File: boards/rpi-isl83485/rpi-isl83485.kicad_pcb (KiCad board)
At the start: 2 copper layers, 25.9 x 15.2 mm, 10 parts, among them J1 RPi, J2 Conn_01x03, J3 JST-GH, U1 ISL83485

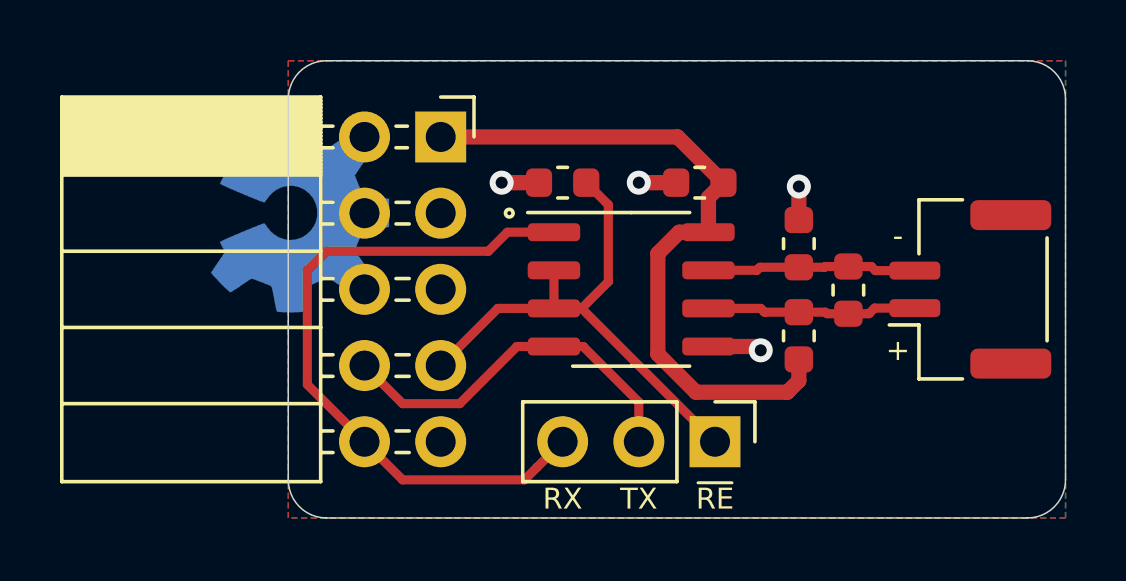
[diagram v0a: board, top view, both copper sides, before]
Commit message: Added FT2232H breakout for programming /boards/ice40hx8k-bg121/
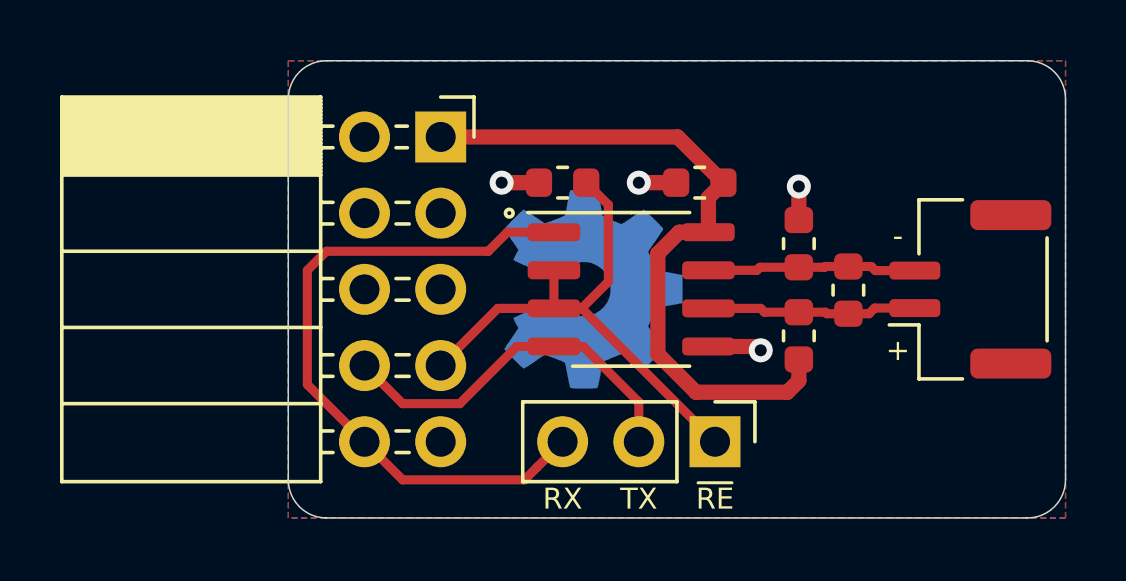
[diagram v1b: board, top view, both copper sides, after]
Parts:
- moved REF** 10.1 mm to (35.6, 25.4)
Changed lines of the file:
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@@
   )
   (module Symbol:OSHW-Symbol_6.7x6mm_Copper (layer B.Cu)
-    (at 25.781 22.86 90)
+    (at 35.56 25.4 90)
     (descr "Open Source Hardware Symbol")
     (tags "Logo Symbol OSHW")
